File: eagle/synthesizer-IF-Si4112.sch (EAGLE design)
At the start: 27 parts, among them U3 SI4112, X24 ECS-TXO-3225, X5 SMA-142-0701-801/806, X6 SMA-142-0701-801/806

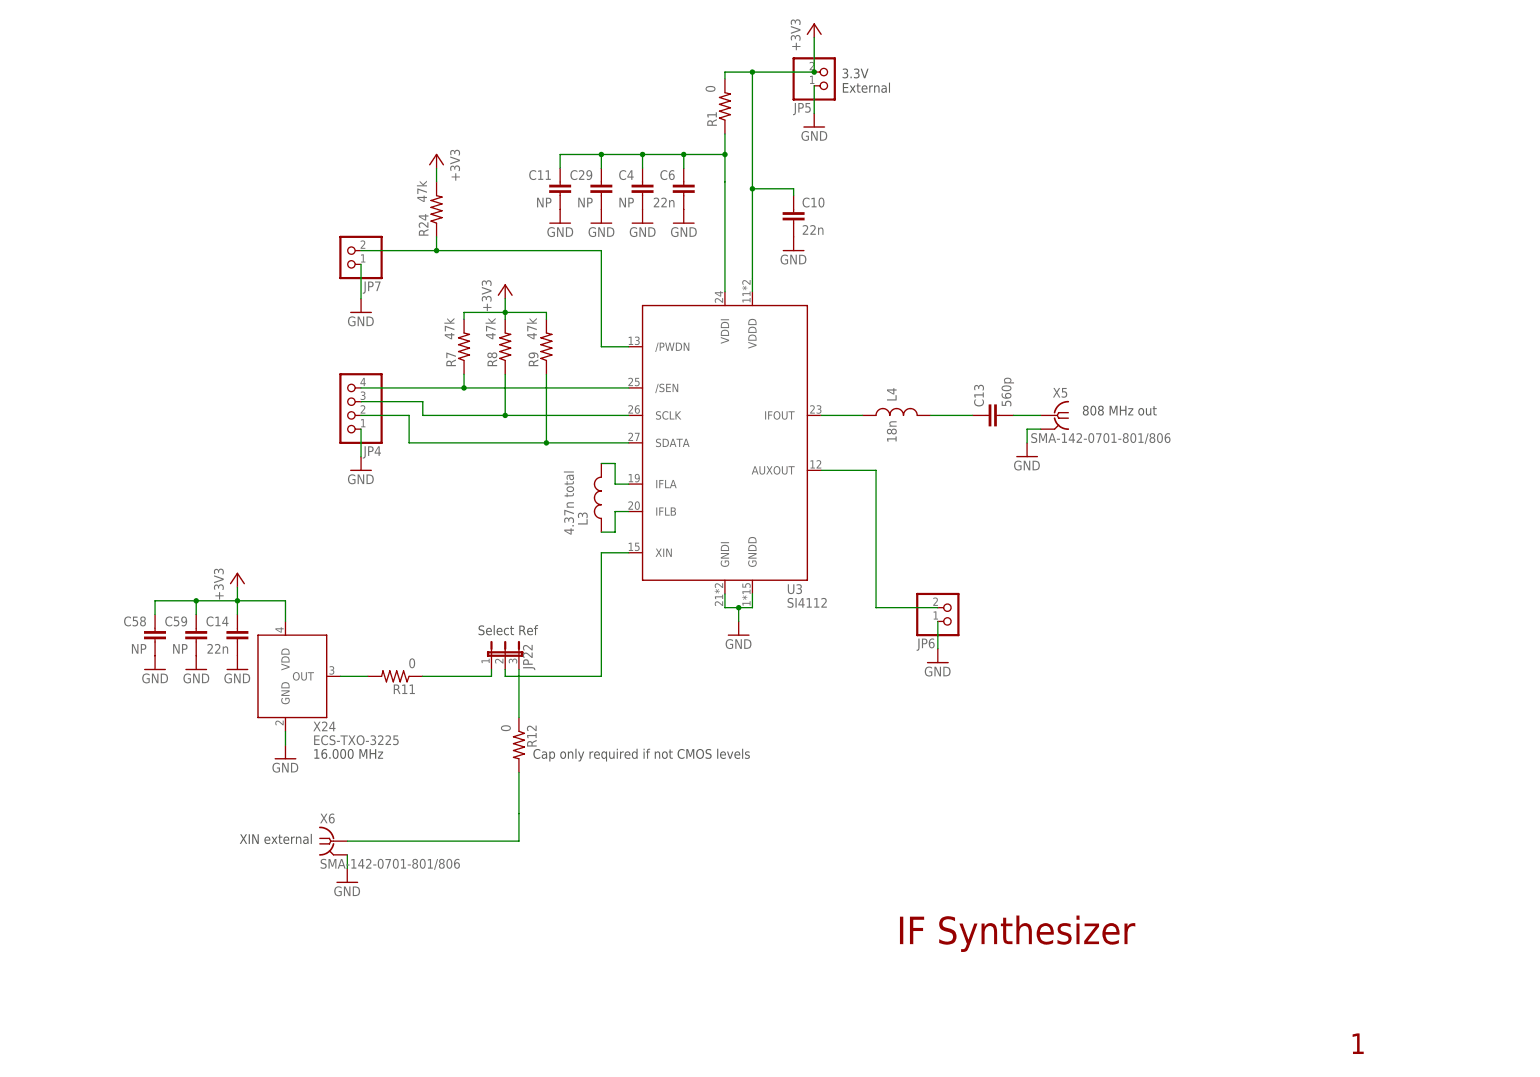
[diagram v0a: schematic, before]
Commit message: Add Si4112 initial layout
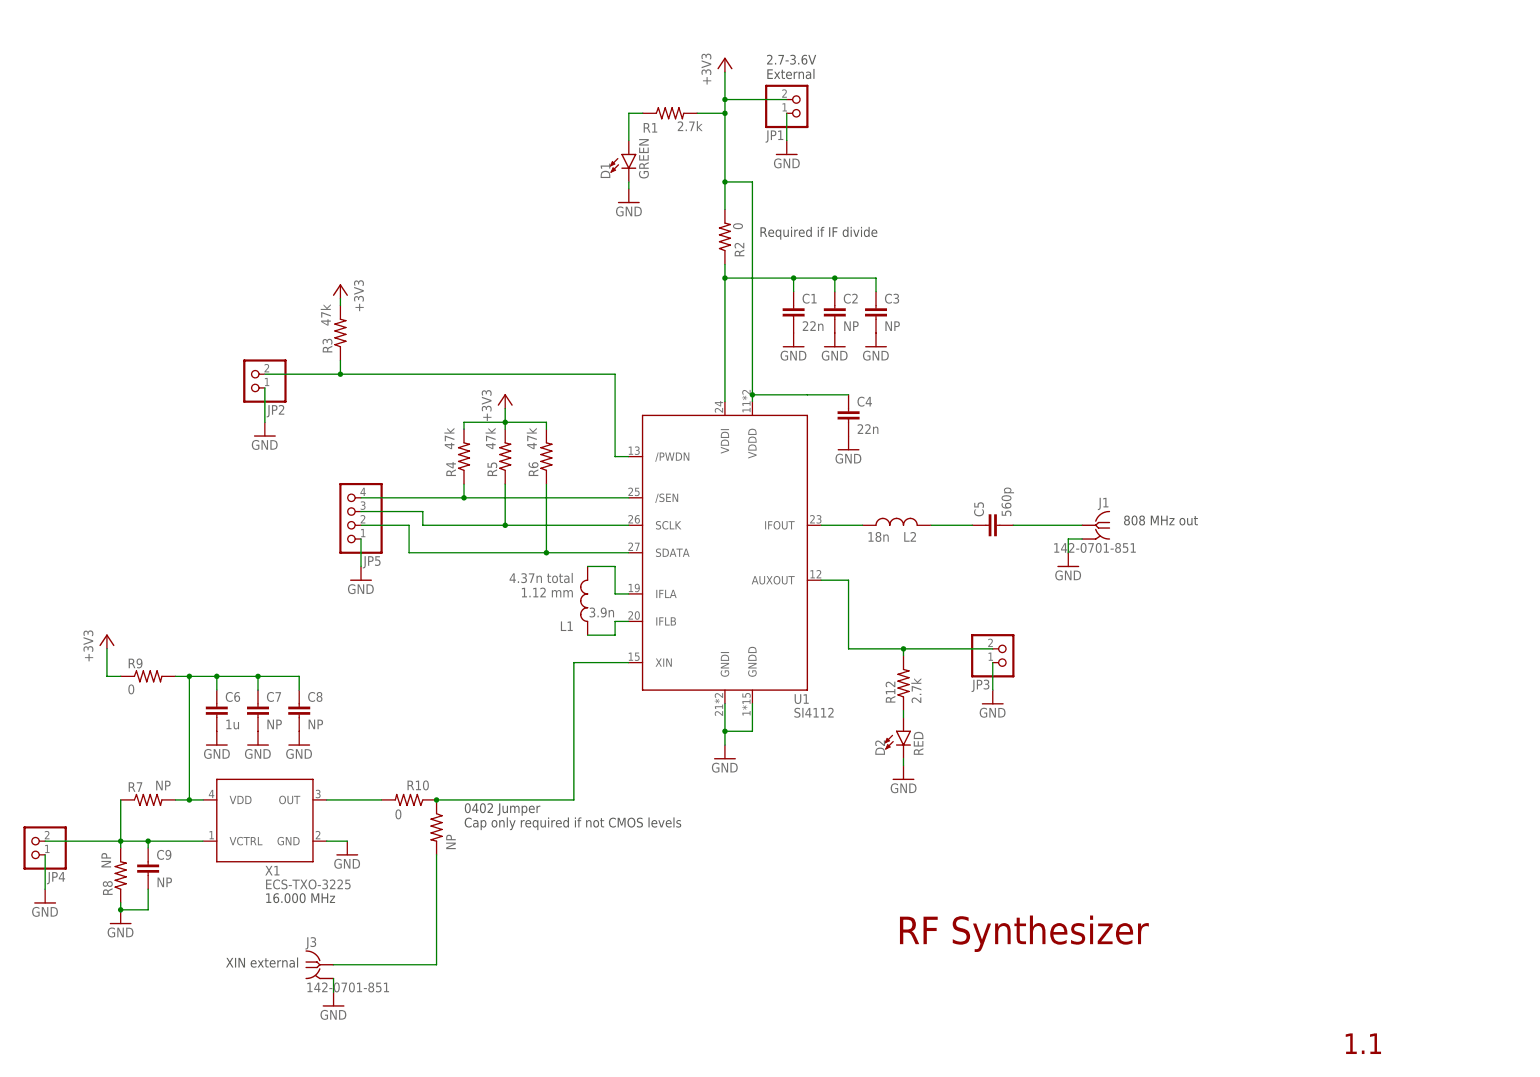
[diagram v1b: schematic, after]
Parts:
- removed C10, C14: 22n, oresat-rcl:C-EU0603-B-NOSILK
- removed C11, C29, C58, C59: NP, oresat-rcl:C-EU0603-B-NOSILK
- removed C13: 560p, oresat-rcl:C-EU0402-B-NOSILK
- removed JP22: (no value), jumper:JP2E
- removed JP6, JP7: (no value), pinhead:PINHD-1X2
- removed L3: 4.37n total, oresat-rcl:L-US0201-B-NOSILK
- removed L4: 18n, oresat-rcl:L-US0201-B-NOSILK
- removed R24: 47k, oresat-rcl:R-US_0402-B-NOSILK
- removed U3: SI4112, U-Silicon-Labs-Si4133-synthesizer:SI4112
- removed X24: ECS-TXO-3225, X-ECS-TXO-TCXO:ECS-TXO-3225
- removed X5, X6: SMA-142-0701-801/806, con-coax:SMA-142-0701-801/806
- added C1: 22n, oresat-rcl:C-EU0603-B-NOSILK
- added C2, C3, C7, C8, C9: NP, oresat-rcl:C-EU0603-B-NOSILK
- added C5: 560p, oresat-rcl:C-EU0402-B-NOSILK
- added D1: GREEN, SparkFun-LED:LED-GREEN0603
- added D2: RED, SparkFun-LED:LED-GREEN0603
- added J1, J3: 142-0701-851, J-Cinch-142-0701-851-SMA-end-launch:142-0701-851
- added JP1, JP2, JP3: (no value), pinhead:PINHD-1X2
- added L1: 3.9n, oresat-rcl:L-US0402-C-NOSILK
- added L2: 18n, oresat-rcl:L-US0402-B-NOSILK
- added R10: 0, oresat-rcl:R-US_0402-B-NOSILK
- added R2: 0, oresat-rcl:R-US_0603-B-NOSILK
- added R3, R4, R5, R6: 47k, oresat-rcl:R-US_0402-B-NOSILK
- added U1: SI4112, U-Silicon-Labs-Si4133-synthesizer:SI4112
- added X1: ECS-TXO-3225, X-ECS-TXO-TCXO:ECS-TXO-3225
- C4: value NP -> 22n
- C6: value 22n -> 1u
- JP4: device pinhead:PINHD-1X4 -> pinhead:PINHD-1X2
- JP5: device pinhead:PINHD-1X2 -> pinhead:PINHD-1X4
- R1, R12: value 0 -> 2.7k; device oresat-rcl:R-US_0402-B-NOSILK -> oresat-rcl:R-US_0603-B-NOSILK
- R11: value 0 -> NP
- R7, R8: value 47k -> NP; device oresat-rcl:R-US_0402-B-NOSILK -> oresat-rcl:R-US_0603-B-NOSILK
- R9: value 47k -> 0; device oresat-rcl:R-US_0402-B-NOSILK -> oresat-rcl:R-US_0603-B-NOSILK
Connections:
- removed net N$1: C13.1, L4.2
- removed net N$15: L4.1, U3.IFOUT
- removed net N$23: JP4.2, R9.1, U3.SDATA
- removed net N$24: JP7.2, R24.1, U3./PWDN
- removed net N$26: JP22.1, R11.1
- removed net N$27: R12.2, X6.1
- removed net N$29: JP22.2, U3.XIN
- removed net N$36: C13.2, X5.1
- removed net N$37: R11.2, X24.OUT
- removed net N$38: JP22.3, R12.1
- new net AUX: JP3.2, R12.2, U1.AUXOUT
- new net IF_OUT: C5.2, J1.RF
- new net N$10: C6.1, C7.1, C8.1, R7.2, R9.2, X1.VDD
- new net N$11: C5.1, L2.2
- new net N$21: D1.A, R1.1
- new net N$4: JP2.2, R3.1, U1./PWDN
- new net N$6: JP5.3, R5.1, U1.SCLK
- new net N$7: JP5.2, R6.1, U1.SDATA
- new net N$9: R10.2, X1.OUT
- new net N$93: C1.1, C2.1, C3.1, R2.1, U1.VDDI
- new net REF_IN: J3.RF, R11.2
- new net XIN: R10.1, R11.1, U1.XIN
- net +3V3: now also C4.1, JP1.2, R2.2, R3.2, R4.2, R5.2, R6.2, R9.1, U1.VDDD; no longer C10.1, C14.1, C58.1, C59.1, JP5.2, R24.2, R7.2, R8.2, R9.2, U3.VDDD, X24.VDD
- net GND: now also C1.2, C2.2, C3.2, C7.2, C8.2, C9.2, D1.C, D2.C, J1.GND, J3.GND, JP1.1, JP2.1, JP3.1, R8.1, U1.GNDD, U1.GNDI, X1.GND; no longer C10.2, C11.2, C14.2, C29.2, C58.2, C59.2, JP6.1, JP7.1, U3.GNDD, U3.GNDI, X24.GND, X5.2, X6.2
- net N$19: now also C9.1, JP4.2, R8.2, X1.VCTRL; no longer JP4.4, U3./SEN
- net N$2: now also L1.2, U1.IFLA; no longer L3.1, U3.IFLA
- net N$22: now also D2.A, R12.1; no longer JP4.3, R8.1, U3.SCLK
- net N$25: now also L2.1, U1.IFOUT; no longer JP6.2, U3.AUXOUT
- net N$3: now also L1.1, U1.IFLB; no longer L3.2, U3.IFLB
- net N$5: now also JP5.4, R4.1, U1./SEN; no longer C11.1, C29.1, C4.1, C6.1, R1.1, U3.VDDI
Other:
- note added: "0402 Jumper Cap only required if not CMOS levels"
- note added: "1.1"
- note added: "2.7-3.6V External"
- note added: "4.37n total 1.12 mm"
- note added: "RF Synthesizer"
- note added: "Required if IF divide"
- note removed: "1"
- note removed: "3.3V External"
- note removed: "Cap only required if not CMOS levels"
- note removed: "IF Synthesizer"
- note removed: "Select Ref"
- moved on the sheet: C4, C6, R1, R12, R7, R8, R9

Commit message: Si4112 layout finish
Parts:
- renumbered R10 to JP6
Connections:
- net N$19 renamed VCTRL
- net N$4 renamed /PWDN
- net N$5 renamed /SEN
- net N$6 renamed SCLK
- net N$7 renamed SDATA
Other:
- note added: "/PWDN High = Enabled (default) Low = Disabled"
- note added: "1"
- note added: "2.7-3.6V External Except w/ on-board TCXO (3.3V req)"
- note added: "AUX OUT Config for lock detect"
- note added: "IF Synthesizer for L band LO"
- note added: "LED ON when: - PLL close to losing lock - PLL not locked"
- note added: "TCXO VCTRL +/- 5ppm min See datasheet"
- note removed: "1.1"
- note removed: "2.7-3.6V External"
- note removed: "RF Synthesizer"
- moved on the sheet: R3
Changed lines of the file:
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@@
 <clearance class="2" value="0.2032"/>
+</class>
+<class number="3" name="RF3" width="0" drill="0">
+<clearance class="3" value="0.3556"/>
 </class>
 </classes>
@@
 <part name="R9" library="oresat-rcl" deviceset="R-US_" device="0603-B-NOSILK" value="0"/>
 <part name="U1" library="U-Silicon-Labs-Si4133-synthesizer" deviceset="SI4112" device=""/>
-<part name="R10" library="oresat-rcl" deviceset="R-US_" device="0402-B-NOSILK" value="0"/>
+<part name="JP6" library="oresat-rcl" deviceset="R-US_" device="0402-B-NOSILK" value="0"/>
 <part name="R11" library="oresat-rcl" deviceset="R-US_" device="0402-B-NOSILK" value="NP"/>
 </parts>
@@
 <sheet>
 <plain>
-<text x="181.61" y="26.67" size="5.08" layer="94">RF Synthesizer</text>
-<text x="264.16" y="6.35" size="3.81" layer="94">1.1</text>
+<text x="176.53" y="26.67" size="5.08" layer="94">IF Synthesizer for L band LO</text>
+<text x="266.7" y="6.35" size="3.81" layer="94">1</text>
 <text x="121.92" y="95.25" size="1.778" layer="96" rot="R180">4.37n total
 1.12 mm</text>
@@
 <text x="223.52" y="104.14" size="1.778" layer="97">808 MHz out</text>
 <text x="71.12" y="24.13" size="1.778" layer="97" rot="R180">XIN external</text>
-<text x="157.48" y="186.69" size="1.778" layer="97">2.7-3.6V
-External</text>
+<text x="157.48" y="186.69" size="1.778" layer="97">2.7-3.6V External
+Except w/ on-board TCXO (3.3V req)</text>
 <text x="64.77" y="34.29" size="1.778" layer="97">16.000 MHz</text>
 <text x="101.6" y="48.26" size="1.778" layer="97">0402 Jumper
 Cap only required if not CMOS levels</text>
+<text x="58.42" y="135.89" size="1.778" layer="97">/PWDN
+High = Enabled (default)
+Low = Disabled</text>
+<text x="17.78" y="49.53" size="1.778" layer="97">TCXO VCTRL
++/- 5ppm min
+See datasheet</text>
+<text x="193.04" y="85.09" size="1.778" layer="97">AUX OUT
+Config for lock detect</text>
+<text x="189.23" y="55.88" size="1.778" layer="97">LED ON when:
+- PLL close to losing lock
+- PLL not locked</text>
 </plain>
 <instances>
@@
 <attribute name="VALUE" x="64.77" y="36.83" size="1.778" layer="96"/>
 </instance>
-<instance part="R3" gate="R" x="78.74" y="139.7" smashed="yes" rot="R90">
-<attribute name="NAME" x="77.2414" y="135.89" size="1.778" layer="95" rot="R90"/>
-<attribute name="VALUE" x="76.962" y="140.97" size="1.778" layer="96" rot="R90"/>
+<instance part="R3" gate="R" x="96.52" y="139.7" smashed="yes" rot="R90">
+<attribute name="NAME" x="95.0214" y="135.89" size="1.778" layer="95" rot="R90"/>
+<attribute name="VALUE" x="94.742" y="140.97" size="1.778" layer="96" rot="R90"/>
 </instance>
 <instance part="GND69" gate="1" x="170.18" y="137.16" smashed="yes">
@@
 <attribute name="VALUE" x="147.32" y="185.42" size="1.778" layer="96" rot="R90"/>
 </instance>
-<instance part="+3V6" gate="G$1" x="78.74" y="148.59" smashed="yes" rot="MR0">
-<attribute name="VALUE" x="81.28" y="143.51" size="1.778" layer="96" rot="MR90"/>
+<instance part="+3V6" gate="G$1" x="96.52" y="148.59" smashed="yes" rot="MR0">
+<attribute name="VALUE" x="99.06" y="143.51" size="1.778" layer="96" rot="MR90"/>
 </instance>
 <instance part="+3V7" gate="G$1" x="109.22" y="128.27" smashed="yes">
@@
 <attribute name="VALUE" x="162.56" y="68.58" size="1.778" layer="96"/>
 </instance>
-<instance part="R10" gate="R" x="91.44" y="53.34" smashed="yes" rot="R180">
+<instance part="JP6" gate="R" x="91.44" y="53.34" smashed="yes" rot="R180">
 <attribute name="NAME" x="95.25" y="56.9214" size="1.778" layer="95" rot="R180"/>
 <attribute name="VALUE" x="90.17" y="51.562" size="1.778" layer="96" rot="R180"/>
@@
 </segment>
 </net>
-<net name="N$5" class="0">
+<net name="/SEN" class="0">
 <segment>
 <pinref part="JP5" gate="A" pin="4"/>
@@
 </segment>
 </net>
-<net name="N$6" class="0">
+<net name="SCLK" class="0">
 <segment>
 <wire x1="132.08" y1="104.14" x2="109.22" y2="104.14" width="0.1524" layer="91"/>
@@
 </segment>
 </net>
-<net name="N$7" class="0">
+<net name="SDATA" class="0">
 <segment>
 <wire x1="132.08" y1="99.06" x2="116.84" y2="99.06" width="0.1524" layer="91"/>
@@
 </segment>
 </net>
-<net name="N$4" class="0">
+<net name="/PWDN" class="0">
 <segment>
 <wire x1="132.08" y1="116.84" x2="129.54" y2="116.84" width="0.1524" layer="91"/>
 <wire x1="129.54" y1="116.84" x2="129.54" y2="132.08" width="0.1524" layer="91"/>
 <pinref part="JP2" gate="G$1" pin="2"/>
-<wire x1="129.54" y1="132.08" x2="78.74" y2="132.08" width="0.1524" layer="91"/>
+<wire x1="129.54" y1="132.08" x2="96.52" y2="132.08" width="0.1524" layer="91"/>
 <pinref part="R3" gate="R" pin="1"/>
-<wire x1="78.74" y1="132.08" x2="64.77" y2="132.08" width="0.1524" layer="91"/>
-<wire x1="78.74" y1="134.62" x2="78.74" y2="132.08" width="0.1524" layer="91"/>
-<junction x="78.74" y="132.08"/>
+<wire x1="96.52" y1="132.08" x2="64.77" y2="132.08" width="0.1524" layer="91"/>
+<wire x1="96.52" y1="134.62" x2="96.52" y2="132.08" width="0.1524" layer="91"/>
+<junction x="96.52" y="132.08"/>
 <pinref part="U1" gate="G$1" pin="/PWDN"/>
 </segment>
@@
 <segment>
 <pinref part="R3" gate="R" pin="2"/>
-<wire x1="78.74" y1="144.78" x2="78.74" y2="146.05" width="0.1524" layer="91"/>
+<wire x1="96.52" y1="144.78" x2="96.52" y2="146.05" width="0.1524" layer="91"/>
 <pinref part="+3V6" gate="G$1" pin="+3V3"/>
 </segment>
@@
 </segment>
 </net>
-<net name="N$19" class="0">
+<net name="VCTRL" class="0">
 <segment>
 <pinref part="JP4" gate="G$1" pin="2"/>
@@
 <segment>
 <pinref part="R11" gate="R" pin="1"/>
-<pinref part="R10" gate="R" pin="1"/>
+<pinref part="JP6" gate="R" pin="1"/>
 <pinref part="U1" gate="G$1" pin="XIN"/>
 <wire x1="132.08" y1="78.74" x2="121.92" y2="78.74" width="0.1524" layer="91"/>
@@
 </segment>
 </net>
-<net name="N$9" class="1">
+<net name="N$9" class="3">
 <segment>
 <pinref part="X1" gate="G$1" pin="OUT"/>
-<pinref part="R10" gate="R" pin="2"/>
+<pinref part="JP6" gate="R" pin="2"/>
 <wire x1="76.2" y1="53.34" x2="86.36" y2="53.34" width="0.1524" layer="91"/>
 </segment>
